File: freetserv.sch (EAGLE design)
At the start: 80 parts, among them IC1 MCP16311-E/MS, IC2 SN75240PW, IC3 TUSB2046BVF, IC4 FT4232HL, IC5 MAX3232ECPW, IC6 MAX3232ECPW, IC7 MAX3232ECPW, IC8 MAX3232ECPW, Q1 12MHz, Q2 6MHz

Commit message: Volker finished the FTDI routing, duplicated it
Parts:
- removed C10, C9: 18pF, resistor:C-EUC0805
- removed IC2: SN75240PW, sn65220_40:SN75240PW
- removed Q1: 12MHz, crystal:CSM-7X-DU
- removed R1, R10, R8, R9: 27, resistor:R-EU_R0805
- removed R11, R12: 10k, resistor:R-EU_R0805
- removed SL1, SL2, SL3, SL4: (no value), con-lstb:MA05-1
- removed USB_IN, USB_RASPI_DATA, USB_RASPI_DATA2: USB_MICROB, ftdi_ft231xq-r:USB_MICROB
- added C100, C101, C102, C103, C104, C105, C106, C107, C108, C109, C110, C111, C112, C113, C114, C115, C116, C47, C489, C519, C54, C55, C56, C57, C58, C59, C60, C61, C62, C63, C64, C65, C66, C67, C68, C69, C70, C71, C72, C73, C74, C75, C76, C77, C78, C79, C80, C81, C859, C869, C89, C90, C91, C92, C93, C94, C95, C96, C97, C98, C99: 0.1uF, resistor:C-EUC0805
- added C502, C53, C879, C889: 4.7uF, resistor:C-EUC0805
- added C629, C829: 3.3uF, resistor:C-EUC0805
- added D1, D2: SN65220, texas1:SN65220
- added FB2, FB2\1, FB2\2, FB3: 330, Wurth_Elektronik_Passive_rev15d:WE-KI_0805A
- added H1, H2, H3, H4: MOUNT-HOLE3.2, holes:MOUNT-HOLE3.2
- added IC10, IC11, IC12, IC13, IC15, IC16, IC17, IC18: MAX3232ECPW, Texas Instruments_By_element14_Batch_1:MAX3232ECPW
- added IC14, IC9: FT4232HL, ftdichip-6:FT4232HL
- added QG1: ASV-12.000MHZ-EJ-T, crystal:XO-XO53
- added R13, R15: 12K / 1%, resistor:R-EU_R0805
- added RN1, RN2: 27, resistor-net:EXBV4V
- added USB_HOST, USB_OUT: USB_MICROB, ftdi_ft231xq-r:USB_MICROB
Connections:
- net +1V8 renamed +1V8-1
- removed net !OVRCUR1: IC3.~OVRCUR1, R11.2
- removed net !OVRCUR2: IC3.~OVRCUR2, R12.2
- removed net !OVRCUR3: IC3.~OVRCUR3
- removed net !OVRCUR4: IC3.~OVRCUR4
- removed net !PWRON1: IC3.~PWRON1
- removed net !PWRON2: IC3.~PWRON2
- removed net !PWRON3: IC3.~PWRON3
- removed net !PWRON4: IC3.~PWRON4
- removed net DX1_N: R9.1, USB_IN.D-
- removed net N$15: C9.1, IC4CORE.XTOUT, Q1.2
- removed net N$16: C10.1, IC4CORE.XTIN, Q1.1
- new net +1V8-2: C59.1, C60.1, C61.1, C629.2, IC9CORE.VCORE@1, IC9CORE.VCORE@2, IC9CORE.VCORE@3, IC9CORE.VREGOUT
- new net +1V8-3: C829.2, C94.1, C95.1, C96.1, IC14CORE.VCORE@1, IC14CORE.VCORE@2, IC14CORE.VCORE@3, IC14CORE.VREGOUT
- new net 12MHZ: IC14CORE.XTIN, IC4CORE.XTIN, IC9CORE.XTIN, QG1.OUT
- new net CTS1E1: IC10.RIN2, U$1G$8.8
- new net CTS1E2: IC15.RIN2, U$1G$12.8
- new net CTS1I1: IC10.ROUT2, IC9A.DB3/CTS
- new net CTS1I2: IC14A.DB3/CTS, IC15.ROUT2
- new net CTS2E1: IC11.RIN2, U$1G$7.8
- new net CTS2E2: IC16.RIN2, U$1G$11.8
- new net CTS2I1: IC11.ROUT2, IC9B.DB3/CTS
- new net CTS2I2: IC14B.DB3/CTS, IC16.ROUT2
- new net CTS3E1: IC12.RIN2, U$1G$6.8
- new net CTS3E2: IC17.RIN2, U$1G$10.8
- new net CTS3I1: IC12.ROUT2, IC9C.DB3/CTS
- new net CTS3I2: IC14C.DB3/CTS, IC17.ROUT2
- new net CTS4E1: IC13.RIN2, U$1G$5.8
- new net CTS4E2: IC18.RIN2, U$1G$9.8
- new net CTS4I1: IC13.ROUT2, IC9D.DB3/CTS
- new net CTS4I2: IC14D.DB3/CTS, IC18.ROUT2
- new net N$100: C103.2, IC16.C2+
- new net N$101: C103.1, IC16.C2-
- new net N$102: C104.2, IC16.V+
- new net N$103: C105.2, IC16.V-
- new net N$104: C107.2, IC17.C1+
- new net N$105: C107.1, IC17.C1-
- new net N$106: C108.2, IC17.C2+
- new net N$107: C108.1, IC17.C2-
- new net N$108: C109.2, IC17.V+
- new net N$109: C110.2, IC17.V-
- new net N$110: C112.2, IC18.C1+
- new net N$111: C112.1, IC18.C1-
- new net N$112: C113.2, IC18.C2+
- new net N$113: C113.1, IC18.C2-
- new net N$114: C114.2, IC18.V+
- new net N$115: C115.2, IC18.V-
- new net N$1355: C519.1, C53.1, FB2.2, IC9CORE.VPLL
- new net N$19: C54.2, IC10.C1+
- new net N$20: C54.1, IC10.C1-
- new net N$23: C55.2, IC10.C2+
- new net N$24: C55.1, IC10.C2-
- new net N$25: C56.2, IC10.V+
- new net N$26: C57.2, IC10.V-
- new net N$27: C67.2, IC11.C1+
- new net N$28: C67.1, IC11.C1-
- new net N$29: C68.2, IC11.C2+
- new net N$30: C68.1, IC11.C2-
- new net N$35: C69.2, IC11.V+
- new net N$36: C70.2, IC11.V-
- new net N$38: C72.2, IC12.C1+
- new net N$41: C72.1, IC12.C1-
- new net N$42: C73.2, IC12.C2+
- new net N$43: C73.1, IC12.C2-
- new net N$5: IC9CORE.REF, R13.2
- new net N$50: C74.2, IC12.V+
- new net N$51: C75.2, IC12.V-
- new net N$5499: C77.2, IC13.C1+
- new net N$55: C77.1, IC13.C1-
- new net N$555: C489.1, C502.1, FB2\1.2, IC9CORE.VPHY
- new net N$56: C78.2, IC13.C2+
- new net N$57: C78.1, IC13.C2-
- new net N$58: C79.2, IC13.V+
- new net N$59: C80.2, IC13.V-
- new net N$64: IC14CORE.REF, R15.2
- new net N$69: C859.1, C879.1, FB2\2.2, IC14CORE.VPHY
- new net N$7: RN2B.2, USB_OUT.D-
- new net N$70: C869.1, C889.1, FB3.2, IC14CORE.VPLL
- new net N$71: C89.2, IC15.C1+
- new net N$72: C89.1, IC15.C1-
- new net N$73: C90.2, IC15.C2+
- new net N$74: C90.1, IC15.C2-
- new net N$75: C91.2, IC15.V+
- new net N$76: C92.2, IC15.V-
- new net N$98: C102.2, IC16.C1+
- new net N$99: C102.1, IC16.C1-
- new net RTS1E1: IC10.DOUT2, U$1G$8.1
- new net RTS1E2: IC15.DOUT2, U$1G$12.1
- new net RTS1I1: IC10.DIN2, IC9A.DB2/RTS
- new net RTS1I2: IC14A.DB2/RTS, IC15.DIN2
- new net RTS2E1: IC11.DOUT2, U$1G$7.1
- new net RTS2E2: IC16.DOUT2, U$1G$11.1
- new net RTS2I1: IC11.DIN2, IC9B.DB2/RTS
- new net RTS2I2: IC14B.DB2/RTS, IC16.DIN2
- new net RTS3E1: IC12.DOUT2, U$1G$6.1
- new net RTS3E2: IC17.DOUT2, U$1G$10.1
- new net RTS3I1: IC12.DIN2, IC9C.DB2/RTS
- new net RTS3I2: IC14C.DB2/RTS, IC17.DIN2
- new net RTS4E1: IC13.DOUT2, U$1G$5.1
- new net RTS4E2: IC18.DOUT2, U$1G$9.1
- new net RTS4I1: IC13.DIN2, IC9D.DB2/RTS
- new net RTS4I2: IC14D.DB2/RTS, IC18.DIN2
- new net RXD1E1: IC10.RIN1, U$1G$8.6
- new net RXD1E2: IC15.RIN1, U$1G$12.6
- new net RXD1I1: IC10.ROUT1, IC9A.DB1/RXD
- new net RXD1I2: IC14A.DB1/RXD, IC15.ROUT1
- new net RXD2E1: IC11.RIN1, U$1G$7.6
- new net RXD2E2: IC16.RIN1, U$1G$11.6
- new net RXD2I1: IC11.ROUT1, IC9B.DB1/RXD
- new net RXD2I2: IC14B.DB1/RXD, IC16.ROUT1
- new net RXD3E1: IC12.RIN1, U$1G$6.6
- new net RXD3E2: IC17.RIN1, U$1G$10.6
- new net RXD3I1: IC12.ROUT1, IC9C.DB1/RXD
- new net RXD3I2: IC14C.DB1/RXD, IC17.ROUT1
- new net RXD4E1: IC13.RIN1, U$1G$5.6
- new net RXD4E2: IC18.RIN1, U$1G$9.6
- new net RXD4I1: IC13.ROUT1, IC9D.DB1/RXD
- new net RXD4I2: IC14D.DB1/RXD, IC18.ROUT1
- new net TXD1E1: IC10.DOUT1, U$1G$8.3
- new net TXD1E2: IC15.DOUT1, U$1G$12.3
- new net TXD1I1: IC10.DIN1, IC9A.DB0/TXD
- new net TXD1I2: IC14A.DB0/TXD, IC15.DIN1
- new net TXD2E1: IC11.DOUT1, U$1G$7.3
- new net TXD2E2: IC16.DOUT1, U$1G$11.3
- new net TXD2I1: IC11.DIN1, IC9B.DB0/TXD
- new net TXD2I2: IC14B.DB0/TXD, IC16.DIN1
- new net TXD3E1: IC12.DOUT1, U$1G$6.3
- new net TXD3E2: IC17.DOUT1, U$1G$10.3
- new net TXD3I1: IC12.DIN1, IC9C.DB0/TXD
- new net TXD3I2: IC14C.DB0/TXD, IC17.DIN1
- new net TXD4E1: IC13.DOUT1, U$1G$5.3
- new net TXD4E2: IC18.DOUT1, U$1G$9.3
- new net TXD4I1: IC13.DIN1, IC9D.DB0/TXD
- new net TXD4I2: IC14D.DB0/TXD, IC18.DIN1
- net !RESET: now also IC14CORE.RESET#, IC9CORE.RESET#
- net +3V3: now also C100.1, C101.1, C106.2, C111.2, C116.2, C47.2, C58.2, C62.1, C63.1, C64.1, C65.1, C66.1, C71.2, C76.2, C81.2, C93.2, C97.1, C98.1, C99.1, FB2.1, FB2\1.1, FB2\2.1, FB3.1, IC10.VCC, IC11.VCC, IC12.VCC, IC13.VCC, IC14CORE.VCCIO@1, IC14CORE.VCCIO@2, IC14CORE.VCCIO@3, IC14CORE.VCCIO@4, IC14CORE.VREGIN, IC15.VCC, IC16.VCC, IC17.VCC, IC18.VCC, IC3.~OVRCUR1, IC3.~OVRCUR2, IC3.~OVRCUR3, IC3.~OVRCUR4, IC9CORE.VCCIO@1, IC9CORE.VCCIO@2, IC9CORE.VCCIO@3, IC9CORE.VCCIO@4, IC9CORE.VREGIN, QG1.TS, QG1.VCC; no longer R11.1, R12.1
- net +5V: no longer USB_RASPI_DATA2.V
- net CTS1E: now also U$1G$4.8; no longer SL1.3
- net CTS2E: now also U$1G$3.8; no longer SL2.3
- net CTS3E: now also U$1G$2.8; no longer SL3.3
- net CTS4E: now also U$1G$1.8; no longer SL4.3
- net D0_N: now also D1.B, RN1B.1; no longer IC2.B, R1.2
- net D0_P: now also D1.A, RN1A.1; no longer IC2.A, R8.2
- net D1_N: now also D2.B, IC3.DM4, RN2B.1; no longer IC2.D, IC3.DM1, R9.2
- net D1_P: now also D2.A, IC3.DP4, RN2A.1; no longer IC2.C, IC3.DP1, R10.2
- net D2_N: now also IC3.DM1; no longer IC3.DM2
- net D2_P: now also IC3.DP1; no longer IC3.DP2
- net D3_N: now also IC3.DM2, IC9CORE.USBDM; no longer IC3.DM3
- net D3_P: now also IC3.DP2, IC9CORE.USBDP; no longer IC3.DP3
- net D4_N: now also IC14CORE.USBDM, IC3.DM3; no longer IC3.DM4
- net D4_P: now also IC14CORE.USBDP, IC3.DP3; no longer IC3.DP4
- net DX0_N: now also RN1B.2, USB_HOST.D-; no longer R1.1, USB_RASPI_DATA.D-
- net DX0_P: now also RN1A.2, USB_HOST.D+; no longer R8.1, USB_RASPI_DATA.D+
- net DX1_P: now also RN2A.2, USB_OUT.D+; no longer R10.1, USB_IN.D+
- net GND: now also C100.2, C101.2, C104.1, C105.1, C106.1, C109.1, C110.1, C111.1, C114.1, C115.1, C116.1, C47.1, C489.2, C502.2, C519.2, C53.2, C56.1, C57.1, C58.1, C59.2, C60.2, C61.2, C62.2, C629.1, C63.2, C64.2, C65.2, C66.2, C69.1, C70.1, C71.1, C74.1, C75.1, C76.1, C79.1, C80.1, C81.1, C829.1, C859.2, C869.2, C879.2, C889.2, C91.1, C92.1, C93.1, C94.2, C95.2, C96.2, C97.2, C98.2, C99.2, D1.GND, D2.GND, IC10.GND, IC11.GND, IC12.GND, IC13.GND, IC14CORE.AGND, IC14CORE.GND@1, IC14CORE.GND@2, IC14CORE.GND@3, IC14CORE.GND@4, IC14CORE.GND@5, IC14CORE.GND@6, IC14CORE.GND@7, IC14CORE.GND@8, IC14CORE.TEST, IC15.GND, IC16.GND, IC17.GND, IC18.GND, IC9CORE.AGND, IC9CORE.GND@1, IC9CORE.GND@2, IC9CORE.GND@3, IC9CORE.GND@4, IC9CORE.GND@5, IC9CORE.GND@6, IC9CORE.GND@7, IC9CORE.GND@8, IC9CORE.TEST, QG1.GND, R13.1, R15.1, U$1G$1.4, U$1G$1.5, U$1G$10.4, U$1G$10.5, U$1G$11.4, U$1G$11.5, U$1G$12.4, U$1G$12.5, U$1G$2.4, U$1G$2.5, U$1G$3.4, U$1G$3.5, U$1G$4.4, U$1G$4.5, U$1G$5.4, U$1G$5.5, U$1G$6.4, U$1G$6.5, U$1G$7.4, U$1G$7.5, U$1G$8.4, U$1G$8.5, U$1G$9.4, U$1G$9.5, USB_HOST.GND, USB_OUT.GND; no longer C10.2, C9.2, IC2.GND@1, IC2.GND@2, IC2.GND@3, IC2.GND@4, SL1.5, SL2.5, SL3.5, SL4.5, USB_IN.GND, USB_RASPI_DATA.GND, USB_RASPI_DATA2.GND
- net RTS1E: now also U$1G$4.1; no longer SL1.4
- net RTS2E: now also U$1G$3.1; no longer SL2.4
- net RTS3E: now also U$1G$2.1; no longer SL3.4
- net RTS4E: now also U$1G$1.1; no longer SL4.4
- net RXD1E: now also U$1G$4.6; no longer SL1.1
- net RXD2E: now also U$1G$3.6; no longer SL2.1
- net RXD3E: now also U$1G$2.6; no longer SL3.1
- net RXD4E: now also U$1G$1.6; no longer SL4.1
- net TXD1E: now also U$1G$4.3; no longer SL1.2
- net TXD2E: now also U$1G$3.3; no longer SL2.2
- net TXD3E: now also U$1G$2.3; no longer SL3.2
- net TXD4E: now also U$1G$1.3; no longer SL4.2
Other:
- note removed: "POWER OUT"
- note removed: "Power Connectors"
- note removed: "USB-IN / OUT"

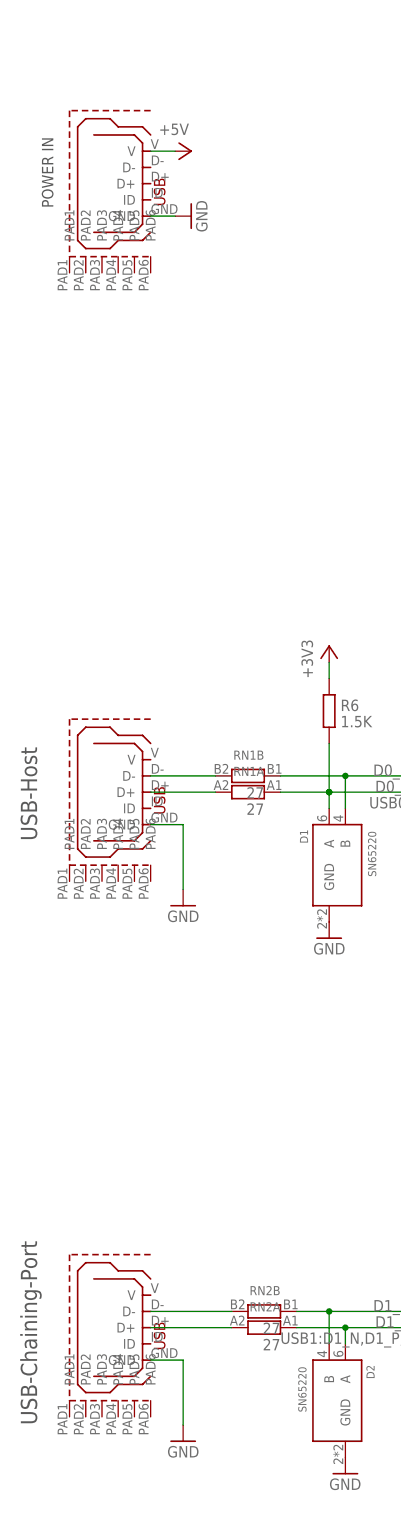
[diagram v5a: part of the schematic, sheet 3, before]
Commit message: replace micro-USB power input with 2-pin header
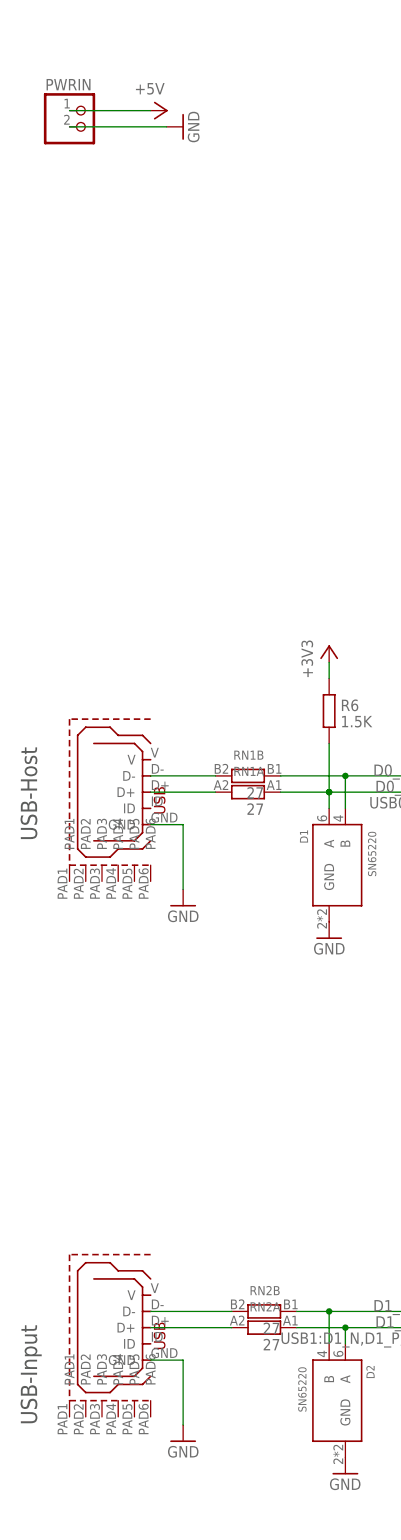
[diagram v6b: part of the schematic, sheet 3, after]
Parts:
- removed USB_RASPI_PWR: USB_MICROB, ftdi_ft231xq-r:USB_MICROB
- added PWRIN: (no value), pinhead:PINHD-1X2
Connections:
- net +5V: now also PWRIN.1; no longer USB_RASPI_PWR.V
- net GND: now also PWRIN.2; no longer USB_RASPI_PWR.GND
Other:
- note added: "USB-Input"
- note removed: "POWER IN"
- note removed: "USB-Chaining-Port"
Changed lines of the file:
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@@
 <?xml version="1.0" encoding="utf-8"?>
 <!DOCTYPE eagle SYSTEM "eagle.dtd">
-<eagle version="7.4.0">
+<eagle version="7.3.0">
 <drawing>
 <settings>
@@
 <setting verticaltext="up"/>
 </settings>
-<grid distance="0.1" unitdist="inch" unit="inch" style="lines" multiple="1" display="no" altdistance="0.05" altunitdist="inch" altunit="inch"/>
+<grid distance="0.1" unitdist="inch" unit="inch" style="lines" multiple="1" display="no" altdistance="0.01" altunitdist="inch" altunit="inch"/>
 <layers>
 <layer number="1" name="Top" color="4" fill="1" visible="no" active="no"/>
@@
 </part>
 <part name="GND10" library="supply1" deviceset="GND" device=""/>
-<part name="USB_RASPI_PWR" library="ftdi_ft231xq-r" deviceset="USB_MICROB" device="">
-<attribute name="PARTNO" value="H11634CT-ND"/>
-</part>
 <part name="C8" library="resistor" deviceset="C-EU" device="C0805" value="3.3uF">
 <attribute name="PARTNO" value="445-7589-1-ND"/>
@@
 <attribute name="PARTNO" value="311-1.5KARCT-ND"/>
 </part>
-<part name="P+1" library="supply1" deviceset="+5V" device=""/>
-<part name="GND2" library="supply1" deviceset="GND" device=""/>
 <part name="U$1" library="stewart_ss73100_046f_dwg" deviceset="SS73100-046F_DWG" device="">
 <attribute name="PARTNO" value="380-1225-ND"/>
@@
 <part name="P+10" library="supply1" deviceset="+3V3" device=""/>
 <part name="P+13" library="supply1" deviceset="+3V3" device=""/>
+<part name="PWRIN" library="pinhead" deviceset="PINHD-1X2" device=""/>
+<part name="P+1" library="supply1" deviceset="+5V" device=""/>
+<part name="GND2" library="supply1" deviceset="GND" device=""/>
 </parts>
 <sheets>
@@
 <sheet>
 <plain>
-<text x="20.32" y="218.44" size="1.778" layer="97" rot="R90">POWER IN</text>
 <wire x1="101.6" y1="248.92" x2="101.6" y2="195.58" width="0.1524" layer="97" style="shortdash"/>
 <wire x1="101.6" y1="195.58" x2="228.6" y2="195.58" width="0.1524" layer="97" style="shortdash"/>
@@
 <wire x1="281.94" y1="177.8" x2="101.6" y2="177.8" width="0.1524" layer="97" style="shortdash"/>
 <text x="104.14" y="172.72" size="2.54" layer="97">USB-Hub</text>
-<text x="17.78" y="27.94" size="2.54" layer="97" rot="R90">USB-Chaining-Port</text>
+<text x="17.78" y="27.94" size="2.54" layer="97" rot="R90">USB-Input</text>
 <text x="17.78" y="119.38" size="2.54" layer="97" rot="R90">USB-Host</text>
 <frame x1="0" y1="0" x2="388.62" y2="261.62" columns="8" rows="5" layer="97"/>
 </plain>
 <instances>
+<instance part="PWRIN" gate="G$1" x="25.4" y="231.14"/>
+<instance part="P+1" gate="1" x="38.1" y="233.68" rot="R270"/>
+<instance part="GND2" gate="1" x="40.64" y="231.14" rot="R90"/>
 <instance part="USB_HOST" gate="G$1" x="35.56" y="125.73">
 <attribute name="PARTNO" x="35.56" y="125.73" size="1.778" layer="96" display="off"/>
@@
 </instance>
 <instance part="GND10" gate="1" x="121.92" y="238.76" rot="R180"/>
-<instance part="USB_RASPI_PWR" gate="G$1" x="35.56" y="220.98">
-<attribute name="PARTNO" x="35.56" y="220.98" size="1.778" layer="96" rot="MR180" display="off"/>
-</instance>
 <instance part="Q2" gate="P" x="147.32" y="144.78" rot="R180">
 <attribute name="PARTNO" x="147.32" y="144.78" size="1.778" layer="96" rot="R270" display="off"/>
@@
 <attribute name="PARTNO" x="154.94" y="139.7" size="1.778" layer="96" rot="R90" display="off"/>
 </instance>
-<instance part="P+1" gate="1" x="41.91" y="227.33" rot="R270"/>
-<instance part="GND2" gate="1" x="41.91" y="217.17" rot="R90"/>
 <instance part="IC1" gate="G$1" x="147.32" y="215.9">
 <attribute name="PARTNO" x="147.32" y="215.9" size="1.778" layer="96" display="off"/>
@@
 <net name="GND" class="0">
 <segment>
+<pinref part="GND2" gate="1" pin="GND"/>
+<pinref part="PWRIN" gate="G$1" pin="2"/>
+<wire x1="38.1" y1="231.14" x2="22.86" y2="231.14" width="0.1524" layer="91"/>
+</segment>
+<segment>
 <pinref part="C20" gate="G$1" pin="1"/>
 <pinref part="GND34" gate="1" pin="GND"/>
@@
 <pinref part="C21" gate="G$1" pin="1"/>
 <pinref part="GND35" gate="1" pin="GND"/>
-</segment>
-<segment>
-<pinref part="GND2" gate="1" pin="GND"/>
-<wire x1="35.56" y1="217.17" x2="39.37" y2="217.17" width="0.1524" layer="91"/>
-<pinref part="USB_RASPI_PWR" gate="G$1" pin="GND"/>
 </segment>
 <segment>
@@
 <net name="+5V" class="2">
 <segment>
+<pinref part="P+1" gate="1" pin="+5V"/>
+<pinref part="PWRIN" gate="G$1" pin="1"/>
+<wire x1="35.56" y1="233.68" x2="22.86" y2="233.68" width="0.1524" layer="91"/>
+</segment>
+<segment>
 <pinref part="IC1" gate="G$1" pin="VIN"/>
 <pinref part="C2" gate="G$1" pin="1"/>
@@
 <wire x1="129.54" y1="220.98" x2="129.54" y2="226.06" width="0.1524" layer="91"/>
 </segment>
-<segment>
-<wire x1="39.37" y1="227.33" x2="35.56" y2="227.33" width="0.1524" layer="91"/>
-<pinref part="P+1" gate="1" pin="+5V"/>
-<pinref part="USB_RASPI_PWR" gate="G$1" pin="V"/>
-</segment>
 </net>
